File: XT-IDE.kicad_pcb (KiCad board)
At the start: 2 copper layers, 114.3 x 106.7 mm, 46 parts, among them J1 CONN_3, J2 CONN_3, J3 CONN_2, J4 CONN_2, J5 INTERRUPT, P6 CONN_1, P7 CONN_1, SW1 I/O ADDR, SW2 ROM OPT, U1 74LS573, U10 74LS688, U11 74LS245, U2 74LS573, U3 74LS245, U4 74LS04, U5 74LS32, U6 74LS04, U7 74LS138, U8 74LS688, U9 28C256

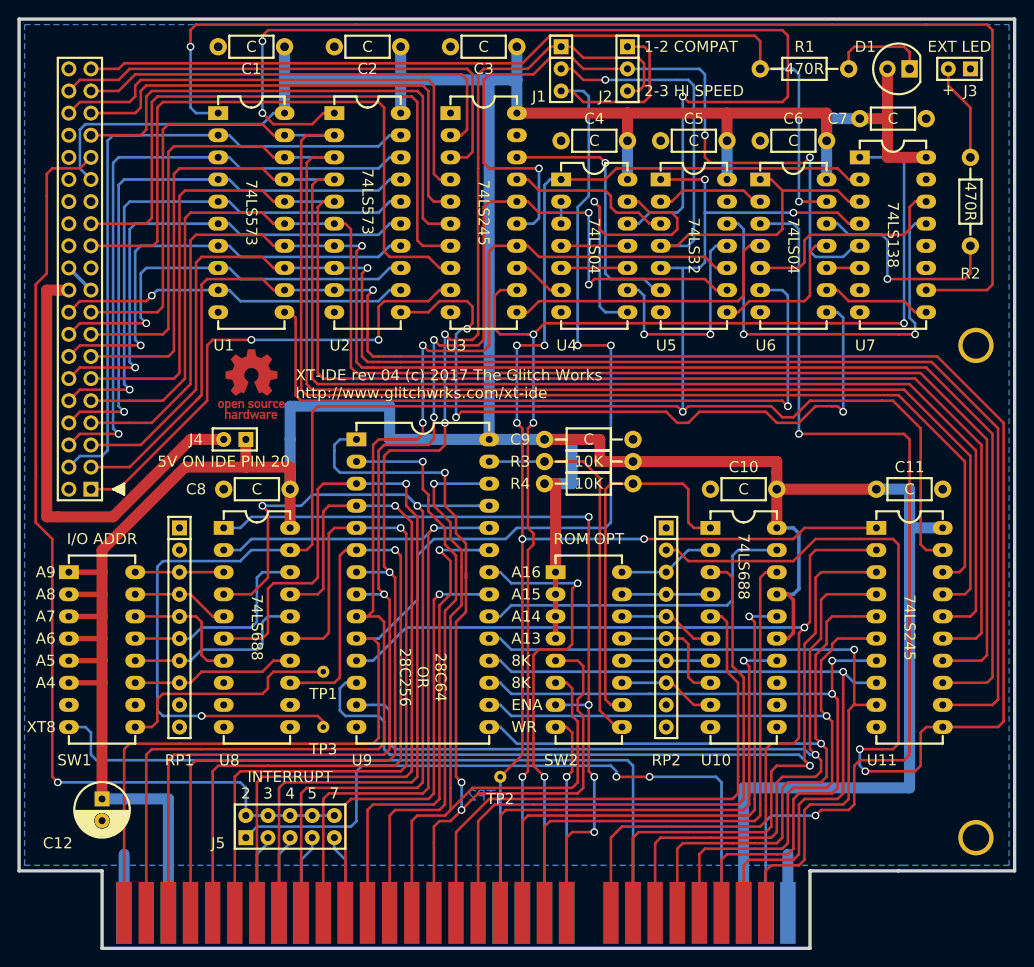
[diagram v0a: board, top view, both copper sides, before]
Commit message: WIP KiCAD 8 upgrade, symbol updates, DRC updates
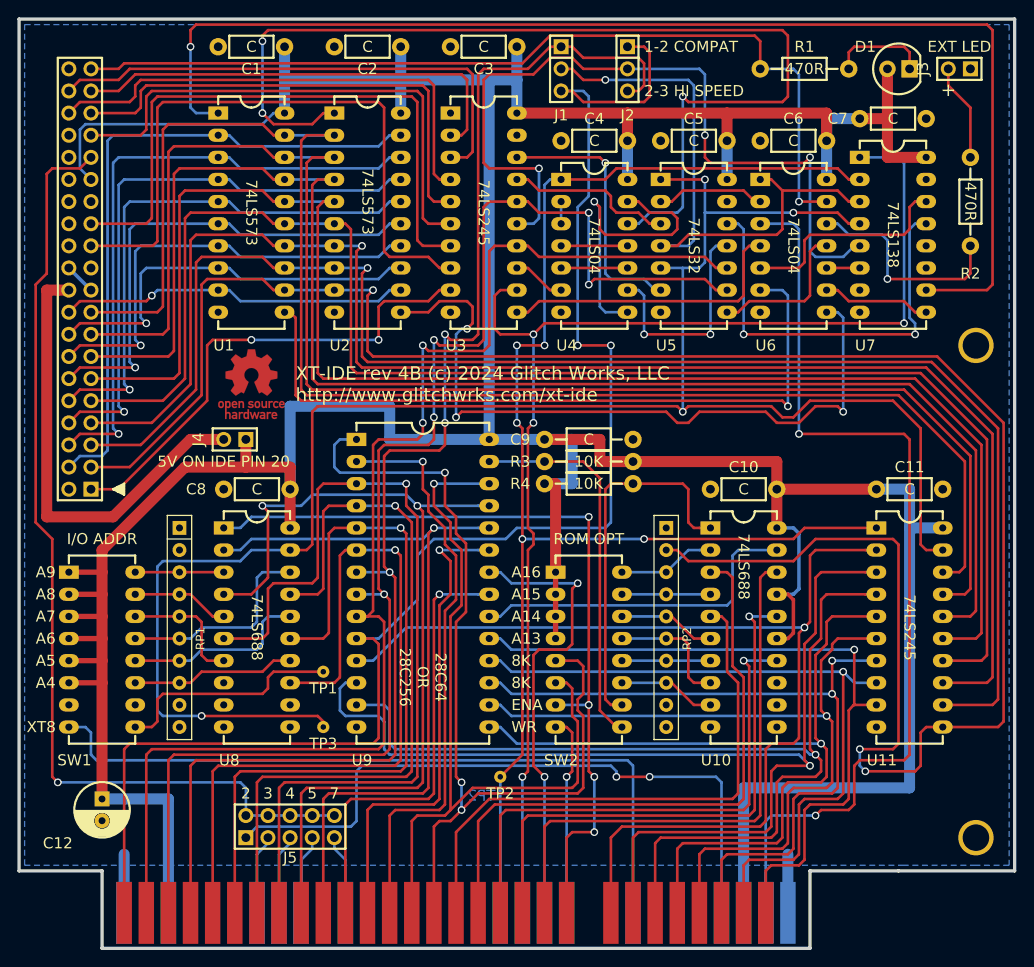
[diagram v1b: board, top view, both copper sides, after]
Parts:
- BUS1: footprint edge_connectors:ISA-8BIT-XT-IDE -> gw_edge_connectors:ISA-8BIT-XT-IDE
- J1, J2: footprint headers_with_detent:1x3 -> gw_headers:1x3
- J3, J4: footprint headers_with_detent:1x2 -> gw_headers:1x2
- J5: footprint headers_with_detent:5x2 -> gw_headers:5x2
- P6, P7: footprint mounting:120mil_no_silkscreen -> gw_mounting:120mil_no_silkscreen
- RP1, RP2: footprint gw_sips:SIP10 -> Resistor_THT:R_Array_SIP10
- TP1, TP2, TP3: footprint testpoints:TH_TESTPOINT -> gw_testpoints:TH_TESTPOINT
- moved RP1 11.4 mm to (95.2, 92.7)
- moved RP2 11.4 mm to (151.1, 92.7)
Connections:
- net /*CS1FX renamed *CS1FX
- net /*CS3FX renamed *CS3FX
- net /*IOR-IDE renamed *IOR-IDE
- net /*IOW-IDE renamed *IOW-IDE
- net /*IOW-ISA renamed *IOW-ISA
- net /*MEMR renamed *MEMR
- net /*RESET renamed *RESET
- net //CS_ROM renamed *CS_ROM
- net /A0-IDE renamed A0-IDE
- net /A0-ISA renamed A0-ISA
- net /A1-IDE renamed A1-IDE
- net /A1-ISA renamed A1-ISA
- net /A10 renamed A10
- net /A11 renamed A11
- net /A12 renamed A12
- net /A2-IDE renamed A2-IDE
- net /A2-ISA renamed A2-ISA
- net /A3 renamed A3
- net /D10 renamed D10
- net /D11 renamed D11
- net /D12 renamed D12
- net /D13 renamed D13
- net /D14 renamed D14
- net /D15 renamed D15
- net /D8 renamed D8
- net /D9 renamed D9
- net /INTRQ renamed Net-(IDE1-INTRQ)
- net /PC-DB0 renamed PC-DB0
- net /PC-DB1 renamed PC-DB1
- net /PC-DB2 renamed PC-DB2
- net /PC-DB3 renamed PC-DB3
- net /PC-DB4 renamed PC-DB4
- net /PC-DB5 renamed PC-DB5
- net /PC-DB6 renamed PC-DB6
- net /PC-DB7 renamed PC-DB7
- net /ROM_WE renamed /ROM_WE
- net /VCC_CF renamed Net-(IDE1-VCC_OPTION)
- net Net-(RP2-Pad7) renamed A14_SW
- net Net-(RP2-Pad8) renamed A13_SW
- IDE1 pad 21: /DMARQ -> unconnected-(IDE1-*DMARQ-Pad21)
- IDE1 pad 27: /IORDY -> unconnected-(IDE1-IORDY-Pad27)
- IDE1 pad 32: /IOCS16 -> unconnected-(IDE1-*IOCS16-Pad32)
- IDE1 pad 34: /PDIAG -> unconnected-(IDE1-PDIAG-Pad34)
- RP1 pad 10: Net-(RP1-Pad10) -> unconnected-(RP1-R9-Pad10)
- RP1 pad 2: Net-(RP1-Pad2) -> unconnected-(RP1-R1-Pad2)
- RP1 pad 9: Net-(RP1-Pad9) -> unconnected-(RP1-R8-Pad9)
- RP2 pad 10: Net-(RP2-Pad10) -> unconnected-(RP2-R9-Pad10)
- RP2 pad 9: Net-(RP2-Pad9) -> unconnected-(RP2-R8-Pad9)
- SW1 pad 10: Net-(SW1-Pad10) -> unconnected-(SW1-Pad10)
- SW1 pad 7: Net-(SW1-Pad7) -> unconnected-(SW1-Pad7)
- U7 pad 11: Net-(U7-Pad11) -> unconnected-(U7-O4-Pad11)
- U7 pad 12: Net-(U7-Pad12) -> unconnected-(U7-O3-Pad12)
- U7 pad 15: Net-(U7-Pad15) -> unconnected-(U7-O0-Pad15)
- U7 pad 7: Net-(U7-Pad7) -> unconnected-(U7-O7-Pad7)
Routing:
- net VCC: track 532.8 -> 527.1 mm
- net A14: track 106.7 -> 105.6 mm
- net D7: track 247.5 -> 246.6 mm
- net /ROM_WE: track 44.1 -> 43.5 mm
- net Net-(J1-Pin_2): track 70.2 -> 69.6 mm
- net Net-(U5-Pad8): track 18.2 -> 17.6 mm
- net /6: track 20.0 -> 19.4 mm
- net /3: track 83.8 -> 83.2 mm
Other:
- net class Default removed
- net class Power removed
- board text added: "GW-XTIDE-4B"
- board text added: "XT-IDE rev 4B (c) 2024 Glitch Works, LLC http://www.glitchwrks.com/xt-ide"
- board text removed: "GW-XTIDE-4"
- board text removed: "XT-IDE rev 04 (c) 2017 The Glitch Works http://www.glitchwrks.com/xt-ide"

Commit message: WIP schematic cleanup, net renames, moving to global labels instead of wire labels, fixing polarities
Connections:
- net *HI_BYTE_OUTPUT renamed *HI_WR_ENA
- net *HI_OUT_DELAYED renamed *HI_WR_DELAYED
- net *IOR-ISA renamed *BIOR
- net *IOW-ISA renamed *BIOW
- net *MEMR renamed *BMEMR
- net *MEMW renamed *BMEMW
- net /3 renamed HI_WR_LOAD
- net /4 renamed *HI_RD_ENA
- net /5 renamed HI_RD_LOAD
- net /IRQ3 renamed BIRQ3
- net /IRQ4 renamed BIRQ4
- net /IRQ5 renamed BIRQ5
- net /IRQ7 renamed BIRQ7
- net A0-ISA renamed BA0
- net A1-ISA renamed BA1
- net A10 renamed BA10
- net A11 renamed BA11
- net A12 renamed BA12
- net A13 renamed BA13
- net A14 renamed BA14
- net A15 renamed BA15
- net A16 renamed BA16
- net A17 renamed BA17
- net A18 renamed BA18
- net A19 renamed BA19
- net A2-ISA renamed BA2
- net A3 renamed BA3
- net A4 renamed BA4
- net A5 renamed BA5
- net A6 renamed BA6
- net A7 renamed BA7
- net A8 renamed BA8
- net A9 renamed BA9
- net AEN renamed BAEN
- net IRQ2 renamed BIRQ2
- net PC-DB0 renamed BD0
- net PC-DB1 renamed BD1
- net PC-DB2 renamed BD2
- net PC-DB3 renamed BD3
- net PC-DB4 renamed BD4
- net PC-DB5 renamed BD5
- net PC-DB6 renamed BD6
- net PC-DB7 renamed BD7
- net RESDRV renamed BRESET
- net /ROM_WE renamed *WE_ROM
